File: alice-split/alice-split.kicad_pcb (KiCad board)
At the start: 2 copper layers, 135 parts, among them SW1 RotaryEncoder_Switch, SW38 SW_PUSH-MX_W_LED, SW39 SW_PUSH-MX_W_LED, SW40 SW_PUSH-MX_W_LED, SW41 SW_PUSH-MX_W_LED, SW42 SW_PUSH-MX_W_LED, SW43 SW_PUSH-MX_W_LED, SW44 SW_PUSH-MX_W_LED, SW45 SW_PUSH-MX_W_LED, SW46 SW_PUSH-MX_W_LED, SW47 SW_PUSH-MX_W_LED, SW48 SW_PUSH-MX_W_LED, SW49 SW_PUSH-MX_W_LED, SW50 SW_PUSH-MX_W_LED, SW51 SW_PUSH-MX_W_LED, SW52 SW_PUSH-MX_W_LED, SW53 SW_PUSH-MX_W_LED, SW54 SW_PUSH-MX_W_LED, SW55 SW_PUSH-MX_W_LED, SW56 SW_PUSH-MX_W_LED, SW57 SW_PUSH-MX_W_LED, SW58 SW_PUSH-MX_W_LED, SW59 SW_PUSH-MX_W_LED, SW60 SW_PUSH-MX_W_LED, SW61 SW_PUSH-MX_W_LED, SW62 SW_PUSH-MX_W_LED, SW63 SW_PUSH-MX_W_LED, SW64 SW_PUSH-MX_W_LED, SW65 SW_PUSH-MX_W_LED, SW66 SW_PUSH-MX_W_LED, SW67 SW_PUSH-MX_W_LED, SW68 SW_PUSH-MX_W_LED, SW69 SW_PUSH-MX_W_LED, SW70 SW_PUSH-MX_W_LED, SW71 SW_PUSH-MX_W_LED, SW72 SW_PUSH-MX_W_LED, SW73 SW_PUSH-MX_W_LED, SW74 SW_PUSH-MX_W_LED, SW75 SW_PUSH-MX_W_LED, SW76 SW_PUSH-MX_W_LED, SW77 SW_PUSH-MX_W_LED, SW78 SW_PUSH-MX_W_LED, SW79 SW_PUSH-MX_W_LED, SW80 SW_PUSH-MX_W_LED, SW81 SW_PUSH-MX_W_LED, SW82 SW_PUSH-MX_W_LED, SW83 SW_PUSH-MX_W_LED, SW84 SW_PUSH-MX_W_LED, SW85 SW_PUSH-MX_W_LED, SW86 SW_PUSH-MX_W_LED, SW87 SW_PUSH-MX_W_LED, SW88 SW_PUSH-MX_W_LED, SW89 SW_PUSH-MX_W_LED, U1 Sparkfun_Pro_Micro

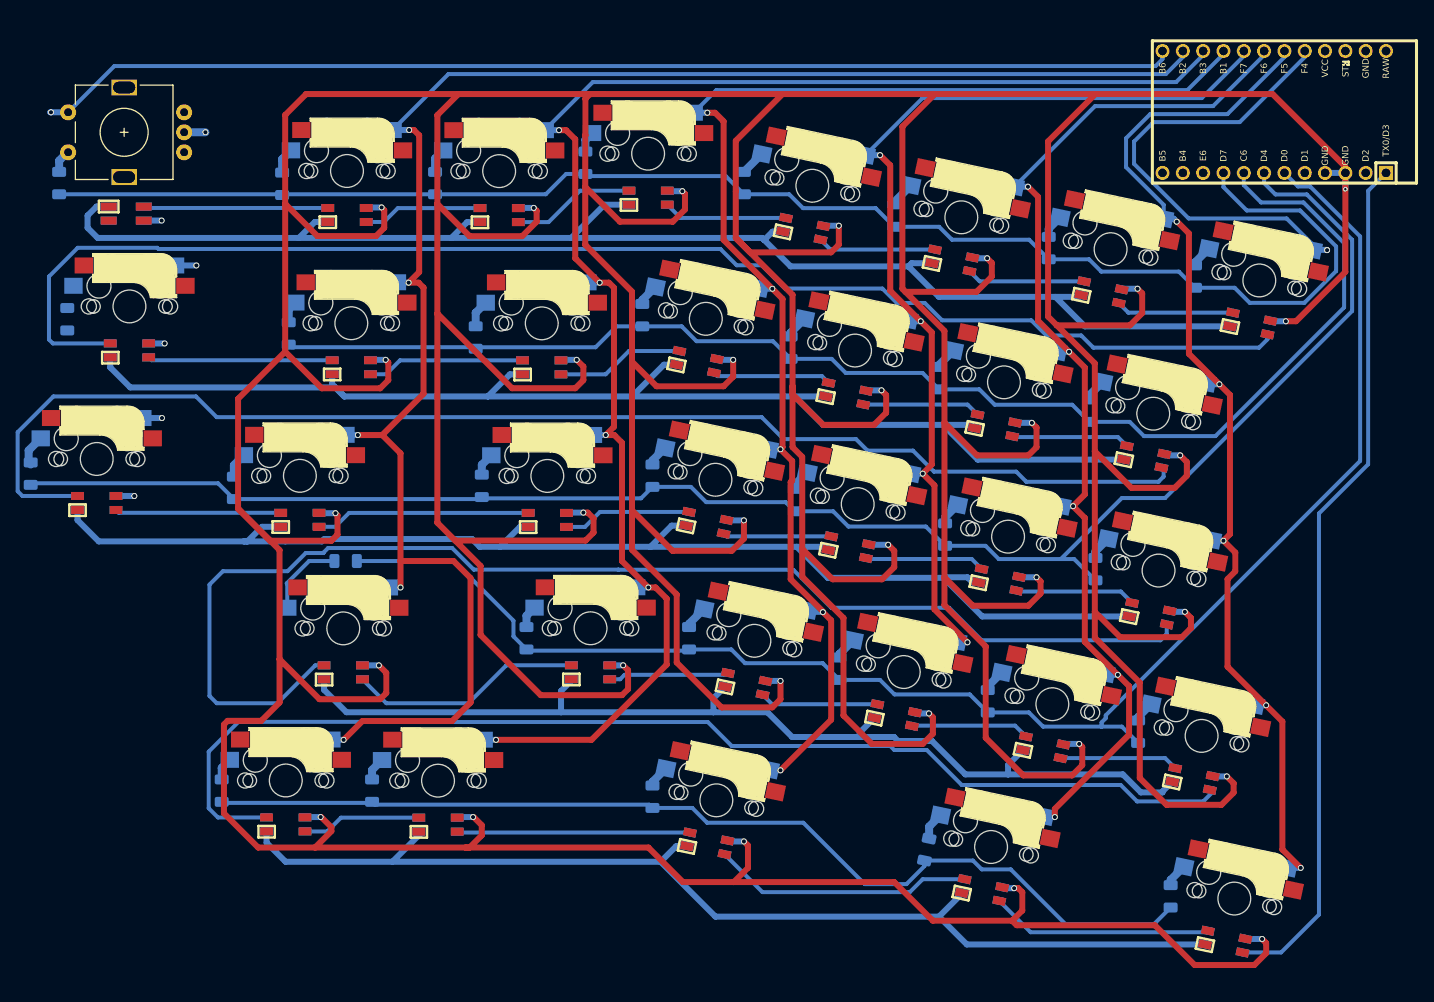
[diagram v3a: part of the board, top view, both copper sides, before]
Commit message: Finished wiring encoder and macros. Fine tuning.
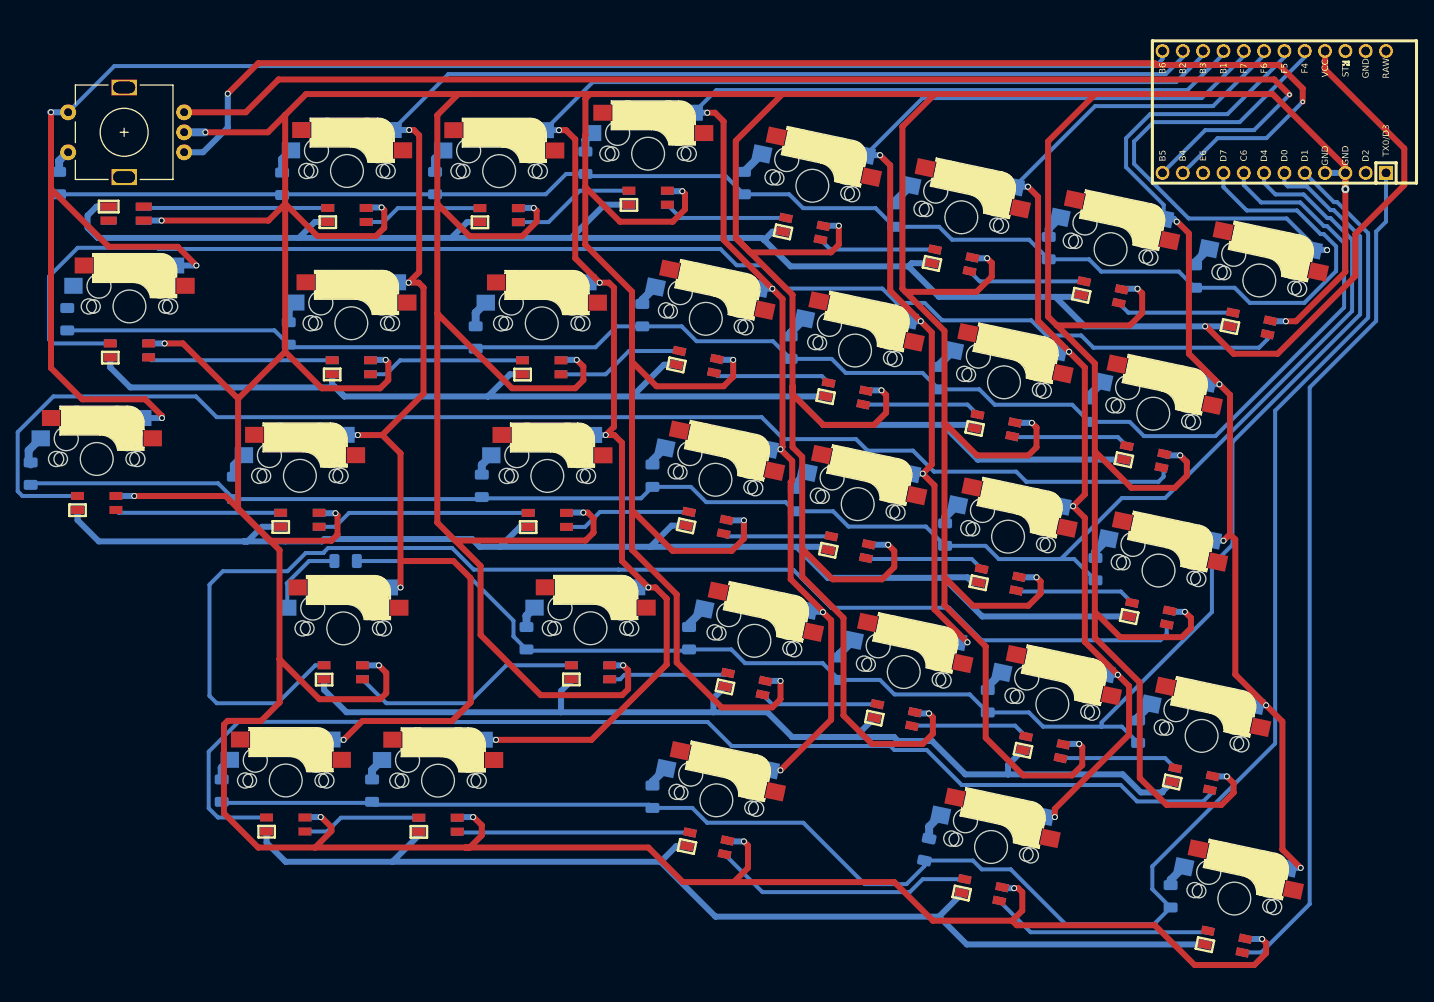
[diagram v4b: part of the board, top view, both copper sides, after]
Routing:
- net ENCA: track 0.00 -> 168.6 mm, vias 0 -> 2
- net ENCB: track 0.00 -> 160.6 mm, vias 0 -> 1
- net ROW0: track 128.8 -> 236.2 mm
- net COL15: track 147.9 -> 218.6 mm
- net VCC: track 764.4 -> 823.4 mm, vias 0 -> 1
- net VDD: track 1335.6 -> 1388.4 mm
- net ROW3: track 170.7 -> 199.2 mm
- net LEDs: track 107.7 -> 106.3 mm
- net ROW1: track 195.8 -> 196.5 mm

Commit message: Moved things around a little bit
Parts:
- moved D1 26.5 mm to (81.5, 48.3)
- moved D10 26.5 mm to (158.0, 52.3)
- moved D11 26.5 mm to (139.2, 48.2)
- moved D12 26.5 mm to (119.4, 45.7)
- moved D19 26.5 mm to (163.6, 72.6)
- moved D23 26.5 mm to (127.8, 84.8)
- moved D24 26.5 mm to (145.5, 87.8)
- moved D25 26.5 mm to (164.3, 92.1)
- moved D26 26.5 mm to (183.1, 96.5)
- moved D27 26.5 mm to (89.4, 95.4)
- moved D29 26.5 mm to (132.3, 105.1)
- moved D30 26.5 mm to (151.1, 108.9)
- moved D31 26.5 mm to (169.7, 113.0)
- moved D36 26.5 mm to (162.1, 131.5)
- moved D39 26.5 mm to (54.6, 65.2)
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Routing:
- net Net-(SW_G1B-DIN): track 158.5 -> 159.3 mm
- net COL14: track 222.5 -> 223.2 mm

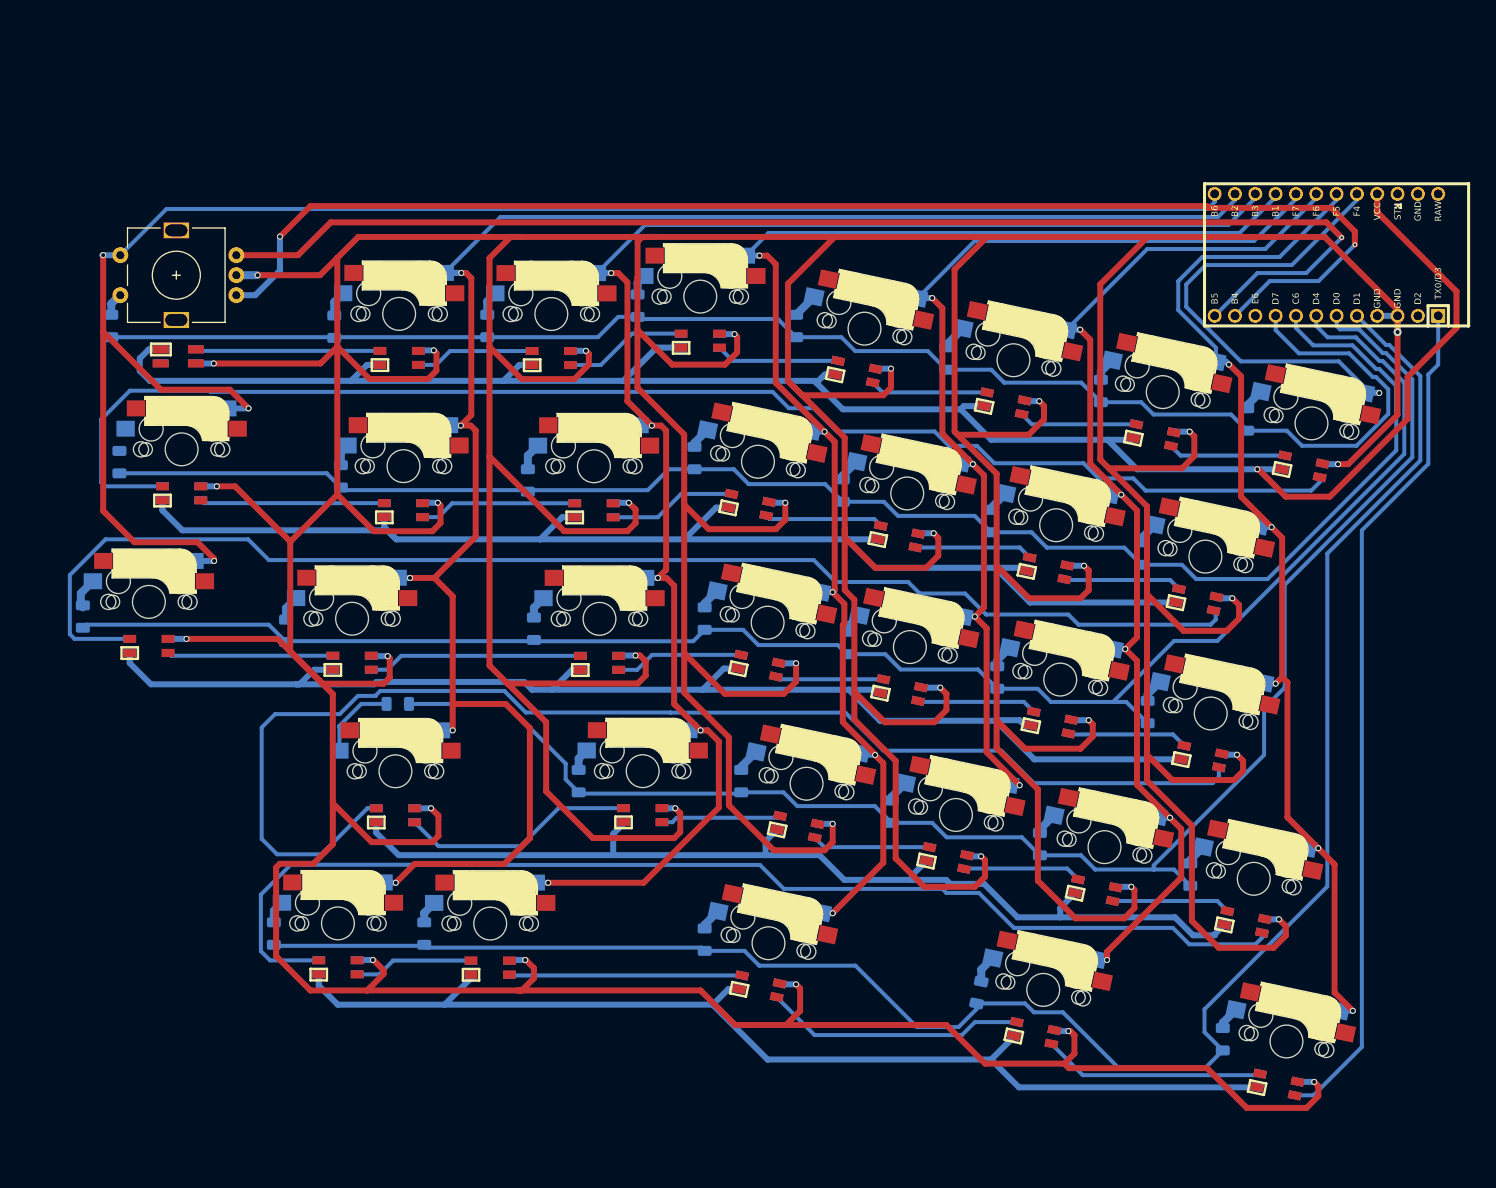
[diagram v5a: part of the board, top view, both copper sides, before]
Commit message: Updating repo after adding the backups to the gitignore file.
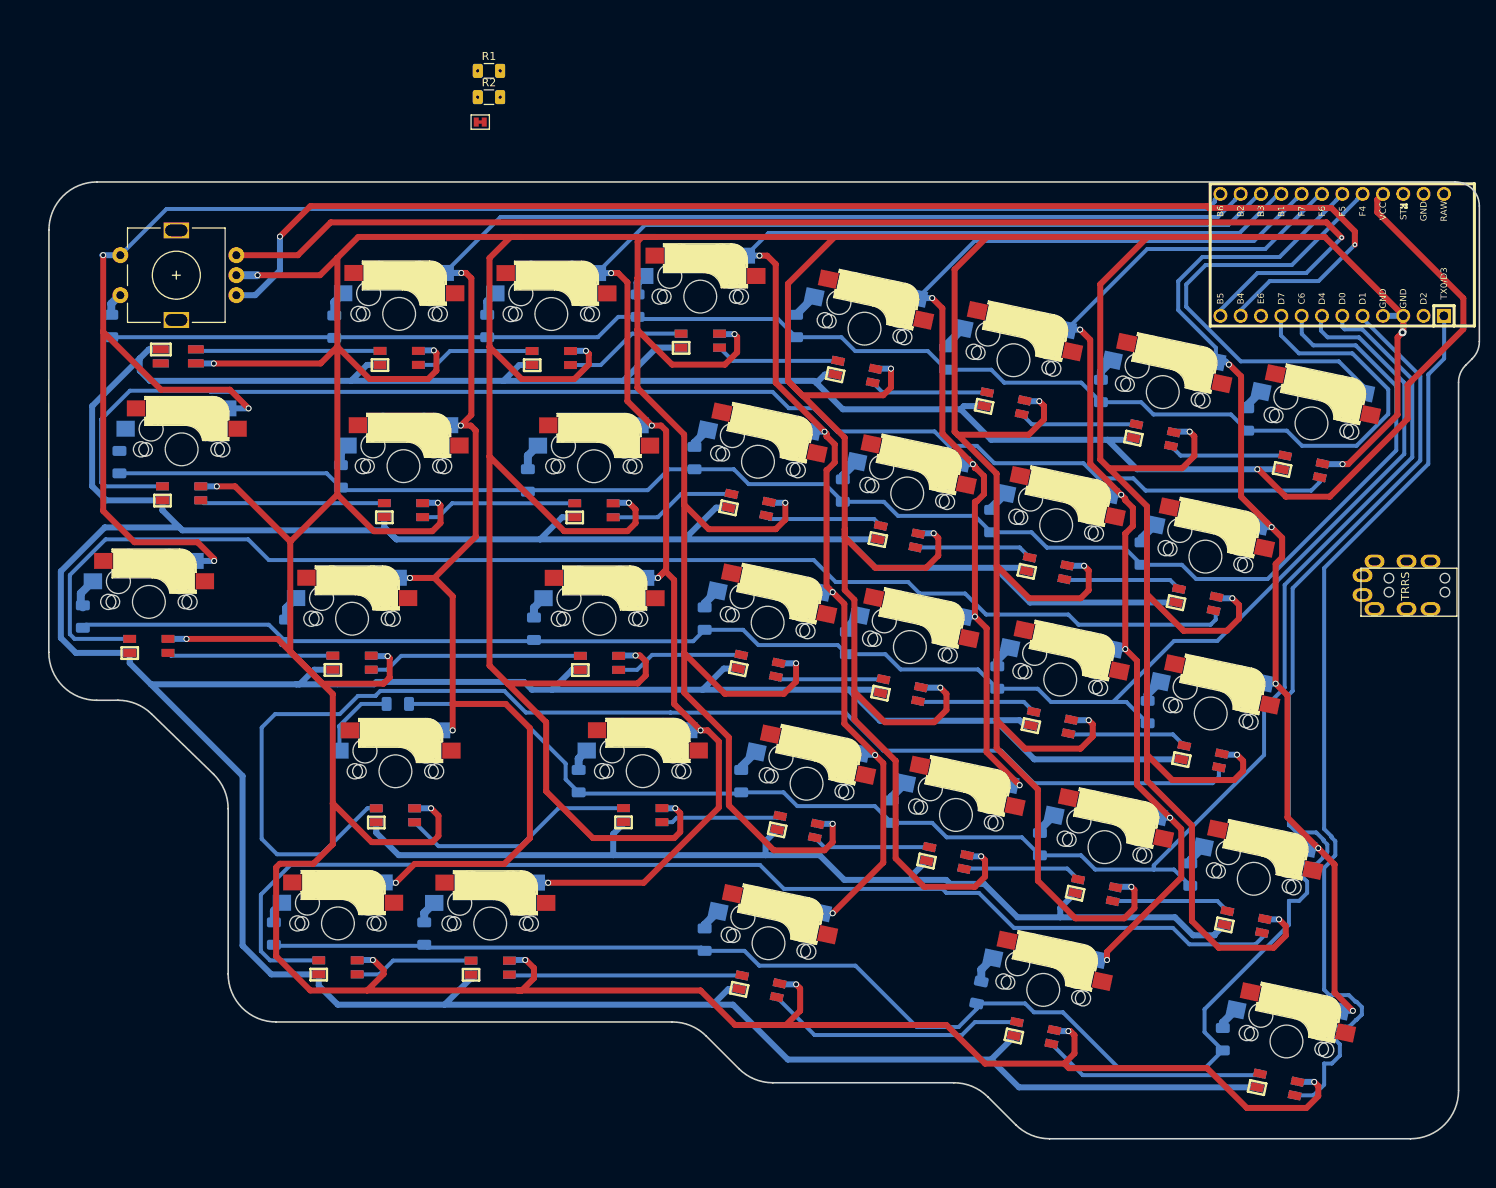
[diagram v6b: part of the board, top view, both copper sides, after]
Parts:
- added J1: MJ-4PP-9-Lily58-cache-Lily58_Pro-rescue, SofleRGB:MJ-4PP-9, F.Cu at (221.8, 81.5)
- added JP1: Jumper-Device, SofleRGB:jumper_data, F.Cu at (99.7, 22.7)
- added R1: R_Small, SofleKeyboard-footprint:R_1206_DoubleSided, F.Cu at (100.8, 16.3)
- added R2: R_Small, SofleKeyboard-footprint:R_1206_DoubleSided, F.Cu at (100.8, 19.6)
- moved U1 0.71 mm to (206.2, 39.3)
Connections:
- U1 pad 2: unconnected-(U1-D0/RX-Pad2) -> DATA
- U1 pad 22: unconnected-(U1-RST-Pad22) -> RESET
- U1 pad 23: unconnected-(U1-GND-Pad23) -> VDD
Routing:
- net VCC: track 823.4 -> 935.6 mm
- net LEDs: track 106.3 -> 115.1 mm
- net ROW0: track 236.2 -> 243.2 mm
- net COL13: track 195.4 -> 197.0 mm
- net COL8: track 58.3 -> 57.1 mm, vias 1 -> 0
- net COL12: track 170.1 -> 171.1 mm
- net VDD: track 1388.6 -> 1389.3 mm
- net ROW1: track 196.5 -> 195.9 mm
- net COL11: track 125.8 -> 126.3 mm
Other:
- board outline added: 178.8 x 119.6 mm
